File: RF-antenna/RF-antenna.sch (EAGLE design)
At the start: 10 parts, among them CON1 UMC_CONNECTORREGULAR, X1 LG_HEADER, X2 LG_HEADER, X3 LG_HEADER, X4 SMA-V

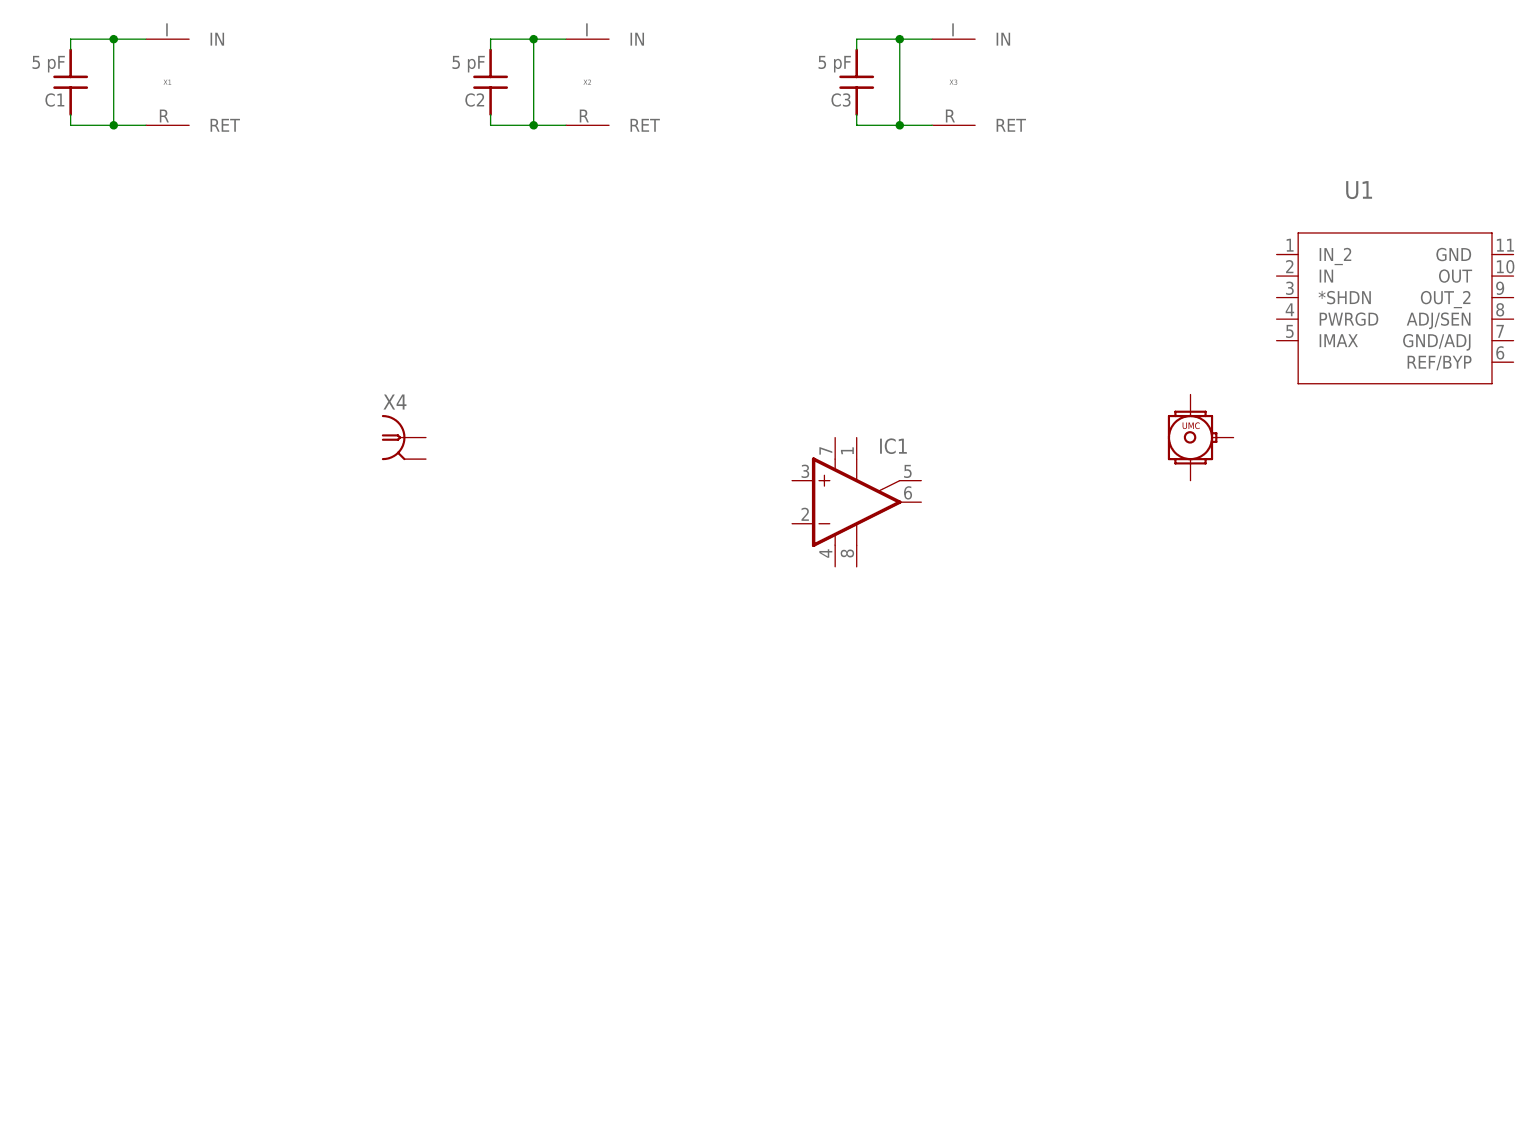
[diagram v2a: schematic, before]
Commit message: Quick Push
Added buffers and minimal schematic.

DSB
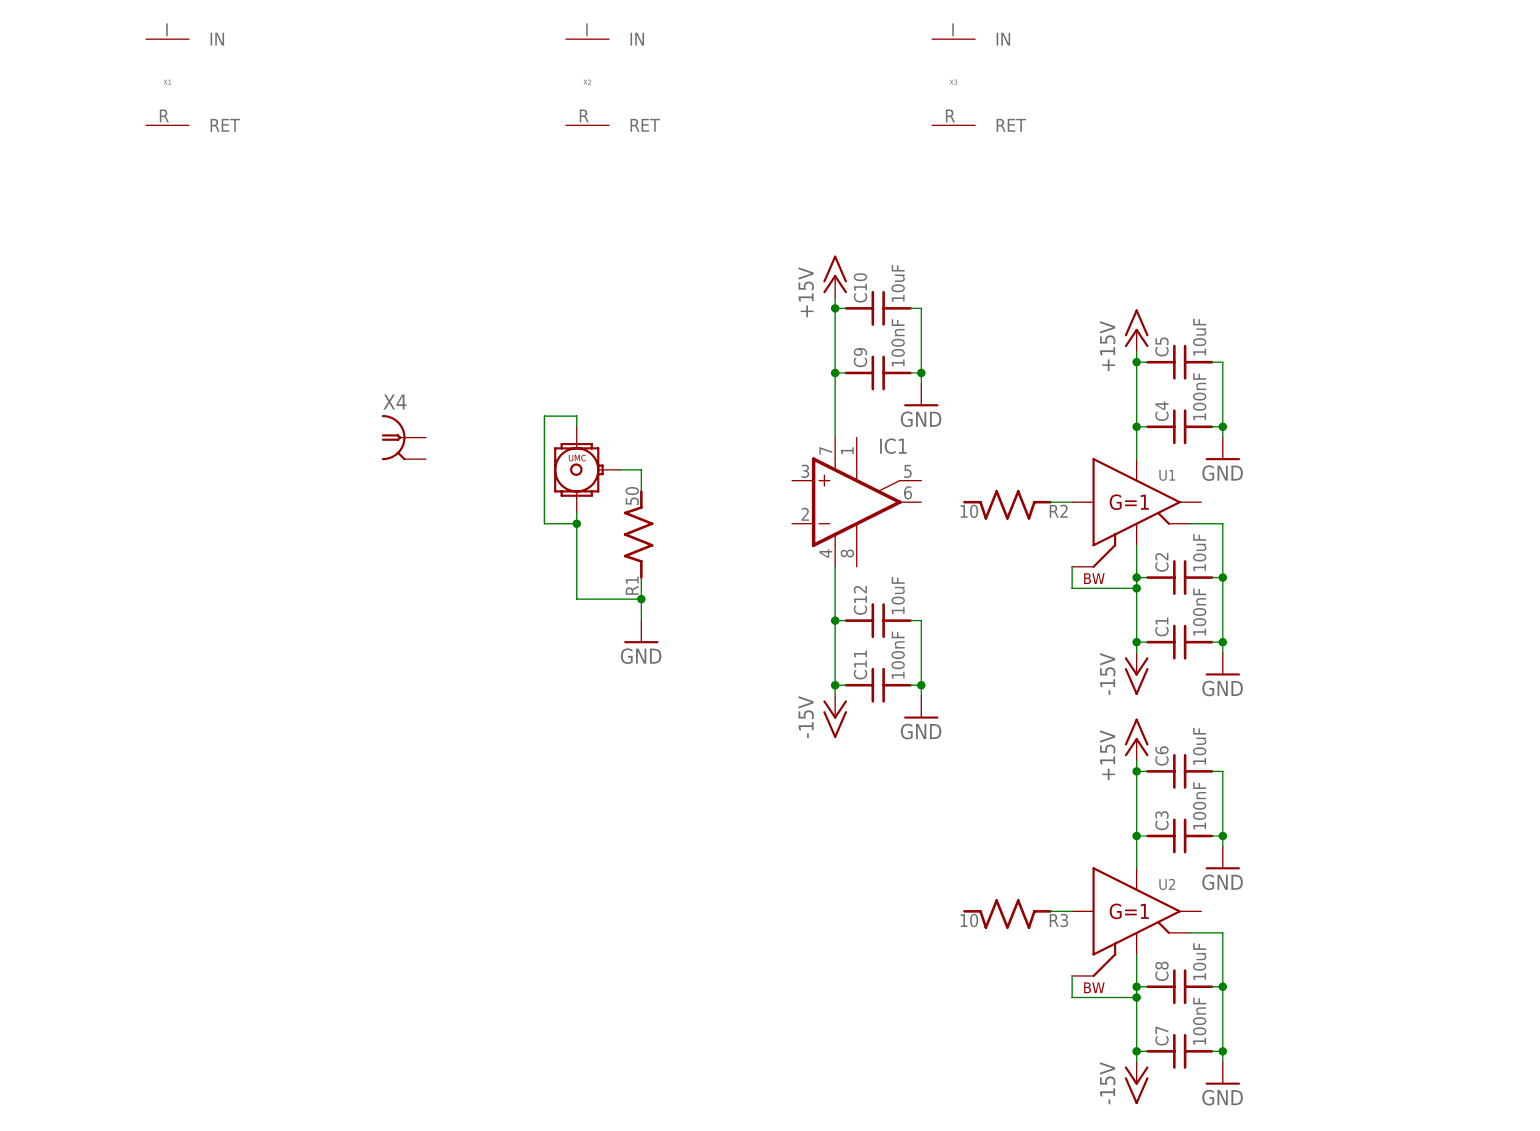
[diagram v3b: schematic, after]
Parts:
- added C10, C12, C5, C6, C8: 10uF, jqi_passives:C_MLCC_SMDCMLCC_1206
- added C11, C4, C7, C9: 100nF, jqi_passives:C_MLCC_SMDCMLCC_0402
- added R1: 50, jqi_passives:R_SMDR0402
- added R2, R3: 10, jqi_passives:R_SMDR0402
- added U2: (no value), texas-instruments-jqi:BUF634U/2K5
- C1, C3: value 5 pF -> 100nF; device jqi_passives:C_MLCC_SMDCMLCC_0603 -> jqi_passives:C_MLCC_SMDCMLCC_0402
- C2: value 5 pF -> 10uF; device jqi_passives:C_MLCC_SMDCMLCC_0603 -> jqi_passives:C_MLCC_SMDCMLCC_1206
- U1: device linear-technology-jqi:LT3065EDDPBF -> texas-instruments-jqi:BUF634U/2K5
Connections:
- removed net N$2: C2.1, C2.2, X2.IN, X2.RET
- removed net N$3: C3.1, C3.2, X3.IN, X3.RET
- new net +15V: C10.1, C3.1, C4.1, C5.1, C6.1, C9.1, IC1.V+, U1.V+, U2.V+
- new net -15V: C1.1, C11.1, C12.1, C2.1, C7.1, C8.1, U1.BW, U1.V-, U2.BW, U2.V-
- new net GND: C1.2, C10.2, C11.2, C12.2, C2.2, C3.2, C4.2, C5.2, C6.2, C7.2, C8.2, C9.2, CON1.P$2, CON1.P$3, R1.1, U1.NC, U2.NC
- new net N$4: CON1.P$1, R1.2
- new net N$6: R2.1, U1.VIN
- net N$1: now also R3.1, U2.VIN; no longer C1.1, C1.2, X1.IN, X1.RET
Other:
- moved on the sheet: C1, C2, C3

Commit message: Zeroth order design
Quick layout for testing with Alessandro.

DSB
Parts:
- removed C10, C12, C6, C8: 10uF, jqi_passives:C_MLCC_SMDCMLCC_1206
- removed C11, C7, C9: 100nF, jqi_passives:C_MLCC_SMDCMLCC_0402
- removed IC1: (no value), opamp-jqi:OPAMP-SO
- removed U1, U2: (no value), texas-instruments-jqi:BUF634U/2K5
- removed X1, X2, X3: LG_HEADER, connector-jqi:LG_HEADER
- removed X4: SMA-V, connector-jqi:SMA-V
- added CON2: UMC_CONNECTORREGULAR, qkdlab_alessandro:UMC_CONNECTORREGULAR
- added JP1: (no value), pinhead:PINHD-1X3
- added LW1, LW2: LITZ_TERM, RFantenna:LITZ_TERM
- added RF: 866, jqi_passives:R_SMDR0603
- added U3: THS3091DDAR, opamp-jqi:THS3091DDAR
- C2: value 10uF -> 100nF; device jqi_passives:C_MLCC_SMDCMLCC_1206 -> jqi_passives:C_MLCC_SMDCMLCC_0402
- C3, C4: value 100nF -> 10uF; device jqi_passives:C_MLCC_SMDCMLCC_0402 -> jqi_passives:C_MLCC_SMDCMLCC_1206
- C5: value 10uF -> 22pF; device jqi_passives:C_MLCC_SMDCMLCC_1206 -> jqi_passives:C_MLCC_SMDCMLCC_0402
- R2: value 10 -> 95.3
- R3: value 10 -> 4.99; device jqi_passives:R_SMDR0402 -> jqi_passives:R_SMDR1206
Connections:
- removed net N$6: R2.1, U1.VIN
- new net N$3: C5.2, R1.2, U3.+IN
- new net N$5: CON1.P$1, LW1.P1, LW2.P1, R3.2, RF.2, U3.OUT
- net +15V: now also C2.1, JP1.3, U3.V+; no longer C10.1, C3.1, C5.1, C6.1, C9.1, IC1.V+, U1.V+, U2.V+
- net -15V: now also C3.1, JP1.1, U3.V-; no longer C11.1, C12.1, C2.1, C7.1, C8.1, U1.BW, U1.V-, U2.BW, U2.V-
- net GND: now also CON2.P$2, CON2.P$3, JP1.2, R2.2, R3.1, U3.ON1, U3.ON2, U3.OPT; no longer C10.2, C11.2, C12.2, C5.2, C6.2, C7.2, C8.2, C9.2, U1.NC, U2.NC
- net N$1: now also R2.1, RF.1, U3.-IN; no longer R3.1, U2.VIN
- net N$4: now also C5.1, CON2.P$1; no longer CON1.P$1, R1.2
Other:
- moved on the sheet: C1, C2, C3, C4, C5, R1, R2, R3
